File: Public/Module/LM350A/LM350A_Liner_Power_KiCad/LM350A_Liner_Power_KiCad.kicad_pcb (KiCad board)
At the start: 2 copper layers, 100 x 100 mm, 23 parts, among them J1 Screw_Terminal_01x04, J2 Screw_Terminal_01x04, J3 Screw_Terminal_01x02, SW1 SS-12D, U1 LM350_TO220

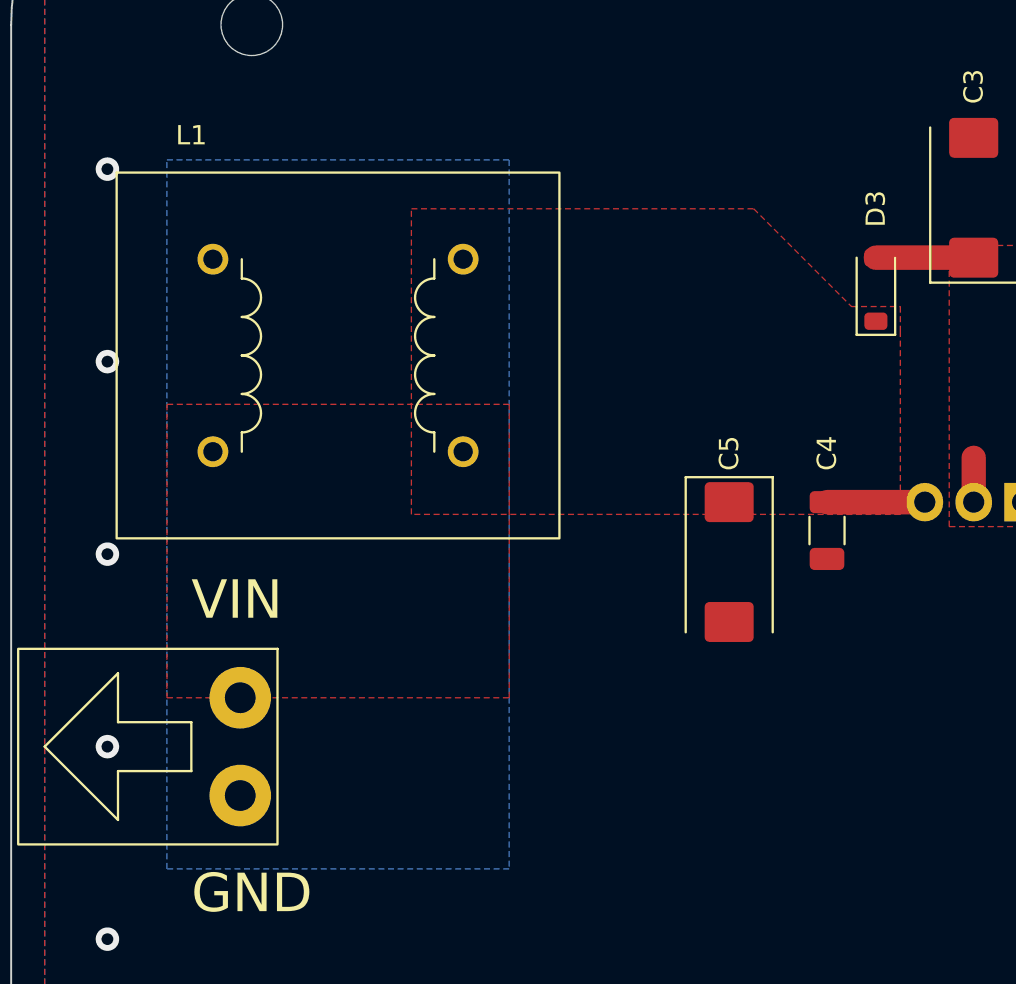
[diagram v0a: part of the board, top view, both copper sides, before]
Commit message: Update LM350 Module
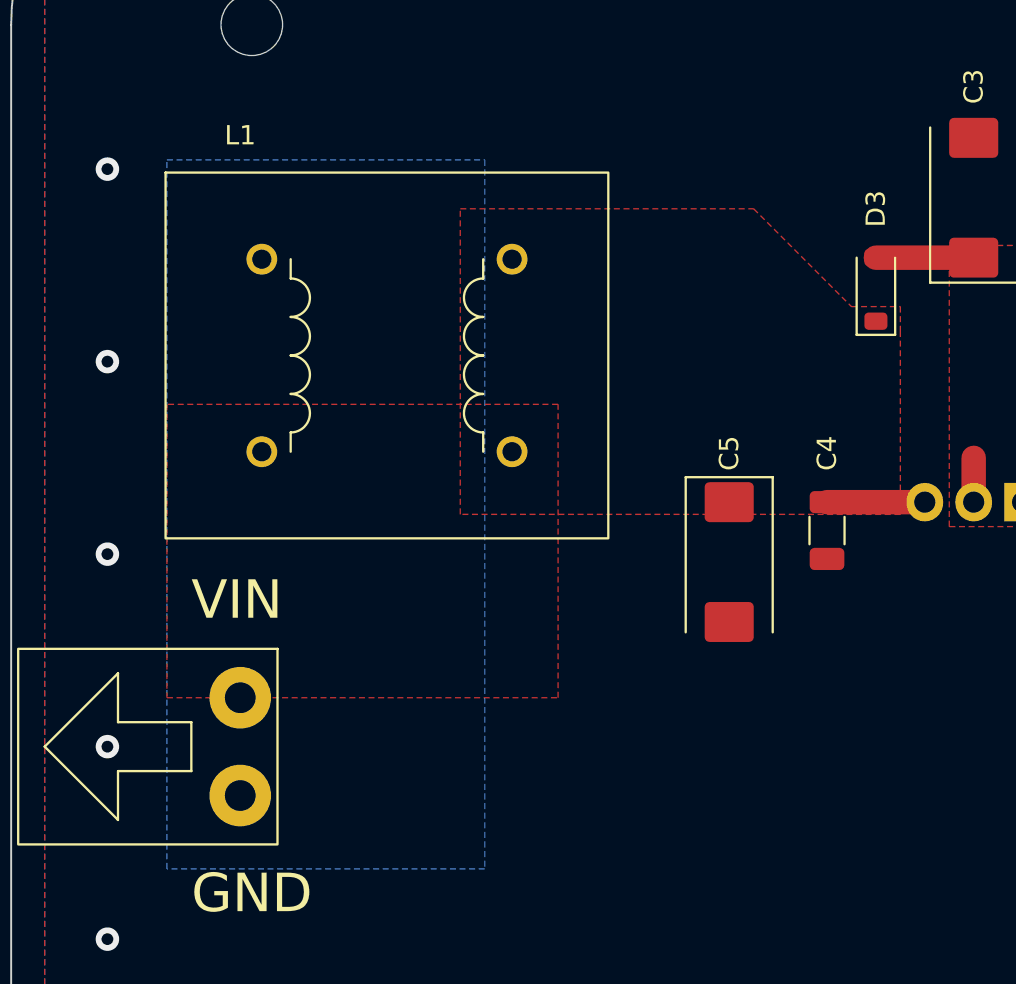
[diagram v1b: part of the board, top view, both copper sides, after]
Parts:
- moved L1 2.54 mm to (121.9, 81.3)
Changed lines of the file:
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@@
   )
   (footprint "Customer_Passive:Inductor_Coupled_THT_UF16" (layer "F.Cu")
-    (at 119.38 81.28)
+    (at 121.92 81.28)
     (property "Sheetfile" "LM350A_Liner_Power_KiCad.kicad_sch")
     (property "Sheetname" "")
@@
       (pts
         (xy 110.49 99.06)
-        (xy 128.27 99.06)
-        (xy 128.27 83.82)
+        (xy 130.81 99.06)
+        (xy 130.81 83.82)
         (xy 110.49 83.82)
       )
@@
     (polygon
       (pts
-        (xy 123.19 73.66)
+        (xy 125.73 73.66)
         (xy 140.97 73.66)
         (xy 146.05 78.74)
@@
         (xy 148.59 80.01)
         (xy 148.59 89.535)
-        (xy 123.19 89.535)
+        (xy 125.73 89.535)
       )
     )
@@
       (pts
         (xy 110.49 71.12)
-        (xy 128.27 71.12)
-        (xy 128.27 107.95)
+        (xy 127 71.12)
+        (xy 127 107.95)
         (xy 110.49 107.95)
       )
